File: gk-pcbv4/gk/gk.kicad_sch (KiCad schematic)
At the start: 19 parts

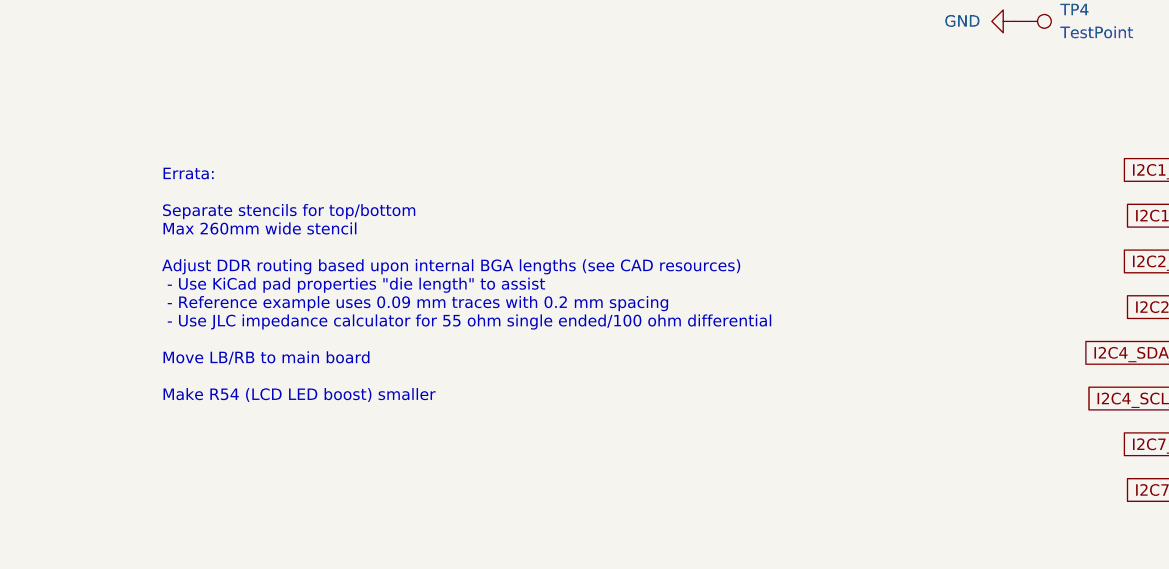
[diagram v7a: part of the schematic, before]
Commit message: move LB/RB to main board
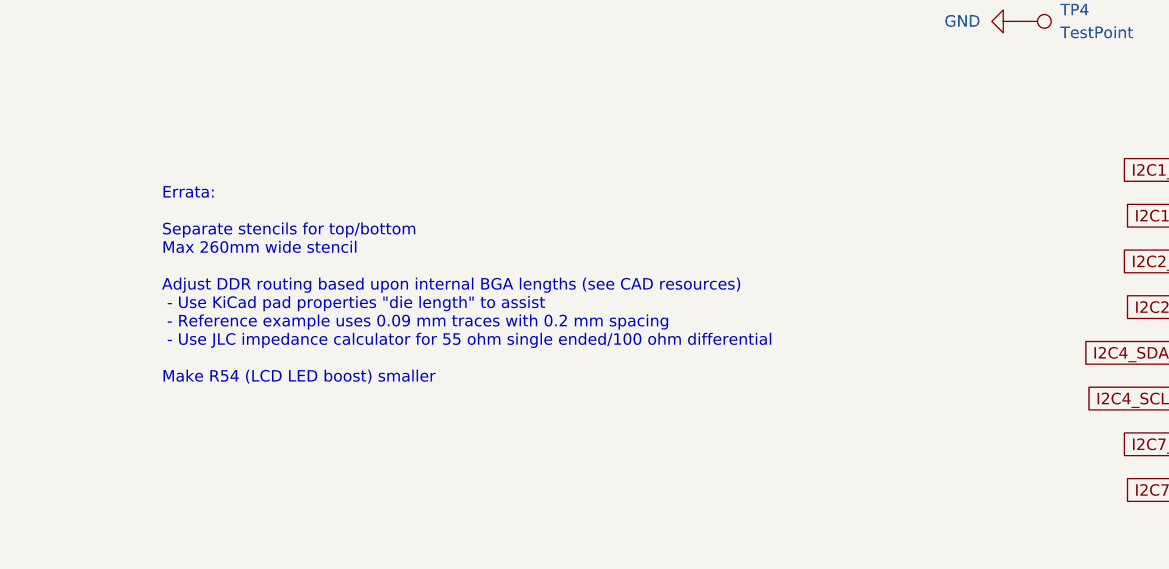
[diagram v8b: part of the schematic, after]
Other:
- note added: "Errata: Separate stencils for top/bottom Max 260mm wide stencil Adjust DDR routing based upon internal BGA lengths (see CAD resources) - Use KiCad pad properties "die length" to assist - Reference example uses 0.09 mm traces with 0.2 mm spacing - Use JLC impedance calculator for 55 ohm single ended/100 ohm differential Make R54 (LCD LED boost) smaller"
- note removed: "Errata: Separate stencils for top/bottom Max 260mm wide stencil Adjust DDR routing based upon internal BGA lengths (see CAD resources) - Use KiCad pad properties "die length" to assist - Reference example uses 0.09 mm traces with 0.2 mm spacing - Use JLC impedance calculator for 55 ohm single ended/100 ohm differential Move LB/RB to main board Make R54 (LCD LED boost) smaller"
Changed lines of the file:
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@@
 		)
 	)
-	(text "Errata:\n\nSeparate stencils for top/bottom\nMax 260mm wide stencil\n\nAdjust DDR routing based upon internal BGA lengths (see CAD resources)\n - Use KiCad pad properties \"die length\" to assist\n - Reference example uses 0.09 mm traces with 0.2 mm spacing\n - Use JLC impedance calculator for 55 ohm single ended/100 ohm differential\n\nMove LB/RB to main board\n\nMake R54 (LCD LED boost) smaller\n\n"
+	(text "Errata:\n\nSeparate stencils for top/bottom\nMax 260mm wide stencil\n\nAdjust DDR routing based upon internal BGA lengths (see CAD resources)\n - Use KiCad pad properties \"die length\" to assist\n - Reference example uses 0.09 mm traces with 0.2 mm spacing\n - Use JLC impedance calculator for 55 ohm single ended/100 ohm differential\n\nMake R54 (LCD LED boost) smaller\n\n"
 		(exclude_from_sim no)
 		(at 104.648 80.01 0)
